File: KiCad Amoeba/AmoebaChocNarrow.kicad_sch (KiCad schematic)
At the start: 6 parts, among them J1 Conn_01x01_Pin, J2 Conn_01x01_Pin, J3 Conn_01x01_Pin, J4 Conn_01x01_Pin, SW1 SW_SPST

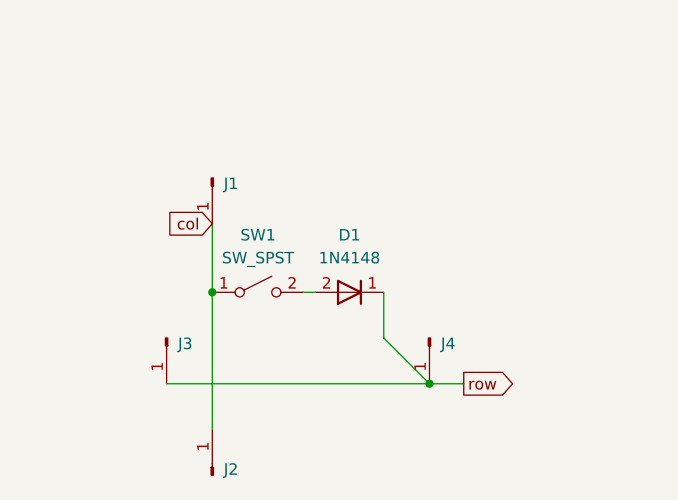
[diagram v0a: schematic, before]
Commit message: feat(amoeba): cleanup
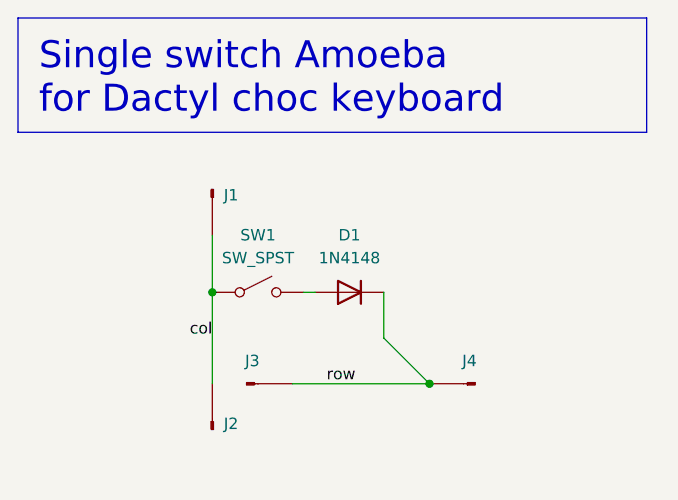
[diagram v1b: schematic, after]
